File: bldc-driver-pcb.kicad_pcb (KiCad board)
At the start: 4 copper layers, 50 x 50 mm, 75 parts, among them IC1 ATSAMD21G18A-AFT, IC2 AS5047P-ATSM, IC3 L6498D, IC4 L6498D, IC5 L6498D, IC6 AD8030ARZ, IC7 AD8030ARZ, J1 FTSH-105-XX-X-DV, J2 43650-0303, J3 G125-MH11205L1P, J4 USB3135-XX-X_REVB, J5 2159310271, Q1 IPD320N20N3GATMA1, Q2 IPD320N20N3GATMA1, Q3 IPD320N20N3GATMA1, Q4 IPD320N20N3GATMA1, Q5 IPD320N20N3GATMA1, Q6 IPD320N20N3GATMA1

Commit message: More routing
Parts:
- added C16: 0.1u, Capacitor_SMD:C_0402_1005Metric, F.Cu at (143.3, 103.6)
- added D1: ~, Diode_SMD:D_0603_1608Metric, B.Cu at (145.5, 108.9)
- added D2: ~, Diode_SMD:D_0603_1608Metric, B.Cu at (145.4, 113.7)
- added D3: ~, Diode_SMD:D_0603_1608Metric, B.Cu at (141.8, 117.9)
- added D4: ~, Diode_SMD:D_0603_1608Metric, B.Cu at (139.8, 122.4)
- added D5: ~, Diode_SMD:D_0603_1608Metric, B.Cu at (117.6, 91.3)
- added D6: ~, Diode_SMD:D_0603_1608Metric, B.Cu at (131.4, 97.8)
- added R31: 10k, Resistor_SMD:R_0603_1608Metric, B.Cu at (143.0, 106.7)
- added R32: 10k, Resistor_SMD:R_0603_1608Metric, B.Cu at (139.9, 112.0)
- added R33: 10k, Resistor_SMD:R_0603_1608Metric, B.Cu at (137.4, 120.8)
- added R34: 10k, Resistor_SMD:R_0603_1608Metric, B.Cu at (138.0, 123.5)
- added R35: 10k, Resistor_SMD:R_0603_1608Metric, B.Cu at (118.8, 97.0)
- added R36: 10k, Resistor_SMD:R_0603_1608Metric, B.Cu at (126.5, 99.0)
- C1, C15, C2, C3, C4, C5, C6, C7, C8, C9, Cboot1, Cboot2, Cboot3, R1, R10, R11, R12, R13, R14, R15, R16, R17, R18, R19, R2, R20, R21, R22, R23, R24, R25, R26, R27, R29, R3, R30, R4, R5, R6, R7, R8, R9: moved to B.Cu
- C10, C11, C12, C14: footprint Capacitor_SMD:C_0603_1608Metric -> Capacitor_SMD:C_0402_1005Metric
- C13: footprint Capacitor_SMD:C_0603_1608Metric -> Capacitor_SMD:C_0402_1005Metric; moved to B.Cu
- FB1: footprint Inductor_SMD:L_0603_1608Metric -> Inductor_SMD:L_0402_1005Metric
- Rshunt1, Rshunt2, Rshunt3: footprint Resistor_SMD:R_0805_2012Metric -> Resistor_SMD:R_1206_3216Metric; moved to B.Cu
- moved R26 110.8 mm to (95.3, 90.8), turned to 180 degrees
- moved R27 110.8 mm to (95.3, 93.3), turned to 180 degrees
- moved R24 103.7 mm to (99.5, 91.0), turned to 180 degrees
- moved R25 100.8 mm to (103.6, 86.9), turned to 180 degrees
- moved R23 99.3 mm to (103.4, 91.7), turned to 180 degrees
- moved R29 99.0 mm to (108.2, 86.4), turned to 180 degrees
- moved R30 99.0 mm to (108.2, 88.9), turned to 180 degrees
- moved Rshunt2 88.9 mm to (128.9, 123.6), turned to 180 degrees
- moved C9 87.1 mm to (107.9, 92.9), turned to 180 degrees
- moved R14 83.6 mm to (119.2, 93.1), turned to 180 degrees
- moved C8 83.4 mm to (111.4, 91.7), turned to 180 degrees
- moved R12 82.7 mm to (120.7, 91.3), turned to 180 degrees
- moved R21 77.9 mm to (127.0, 119.5), turned to 180 degrees
- moved R22 77.6 mm to (127.0, 121.1)
- moved Rshunt1 75.5 mm to (136.6, 106.0), turned to 90 degrees
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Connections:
- IC3 pad 2: /Microcontroller/TCC0_WO1 -> /Microcontroller/TCC0_WO4
- IC4 pad 1: /Microcontroller/TCC0_WO2 -> /Microcontroller/TCC0_WO1
- IC4 pad 2: /Microcontroller/TCC0_WO4 -> /Microcontroller/TCC0_WO5
- IC5 pad 1: /Microcontroller/TCC0_WO5 -> /Microcontroller/TCC0_WO2
- Q2 pad 3: Net-(Q2-S) -> /Current Sensing/CSA_1_IN+
- Q4 pad 3: Net-(Q4-S) -> /Current Sensing/CSA_2_IN+
- Q6 pad 3: Net-(Q6-S) -> /Current Sensing/CSA_3_IN+
- R18 pad 2: /Current Sensing/CSA_2_IN- -> GND
- R23 pad 1: /Current Sensing/CSA_3_IN- -> GND
- R3 pad 1: /Current Sensing/CSA_1_IN- -> GND
- Rshunt1 pad 1: Net-(Q2-S) -> /Current Sensing/CSA_1_IN+
- Rshunt1 pad 2: /Current Sensing/CSA_1_IN+ -> GND
- Rshunt2 pad 1: Net-(Q4-S) -> /Current Sensing/CSA_2_IN+
- Rshunt2 pad 2: /Current Sensing/CSA_2_IN+ -> GND
- Rshunt3 pad 1: Net-(Q6-S) -> /Current Sensing/CSA_3_IN+
- Rshunt3 pad 2: /Current Sensing/CSA_3_IN+ -> GND
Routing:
- net +3V3: track 62.0 -> 110.4 mm, vias 5 -> 10
- net /Microcontroller/TCC0_WO1: track 0.00 -> 36.8 mm, vias 0 -> 3
- net /Microcontroller/TCC0_WO5: track 0.00 -> 34.9 mm, vias 0 -> 1
- net GND: track 30.1 -> 56.2 mm, vias 15 -> 70
- net /Microcontroller/TCC0_WO6: track 0.00 -> 22.5 mm, vias 0 -> 1
- net /Current Sensing/CSA_2_VOUT: track 0.00 -> 22.4 mm, vias 0 -> 1
- net /Microcontroller/TCC0_WO2: track 0.00 -> 21.4 mm, vias 0 -> 1
- net /Microcontroller/TCC0_WO0: track 0.00 -> 21.2 mm, vias 0 -> 1
- net VBUS: track 61.3 -> 79.2 mm, vias 0 -> 4
- net /Current Sensing/CSA_1_VOUT: track 0.00 -> 16.6 mm, vias 0 -> 1
- net /Three-Phase Inverter/HALF_BRIDGE_1_OUT: track 24.9 -> 41.3 mm, vias 0 -> 1
- net /Microcontroller/TCC0_WO4: track 0.00 -> 15.9 mm, vias 0 -> 1
- net Net-(D2-A): track 0.00 -> 14.1 mm, vias 0 -> 1
- net Net-(IC4-LVG): track 0.00 -> 12.9 mm
- net /Three-Phase Inverter/HALF_BRIDGE_2_OUT: track 27.3 -> 38.7 mm, vias 0 -> 1
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
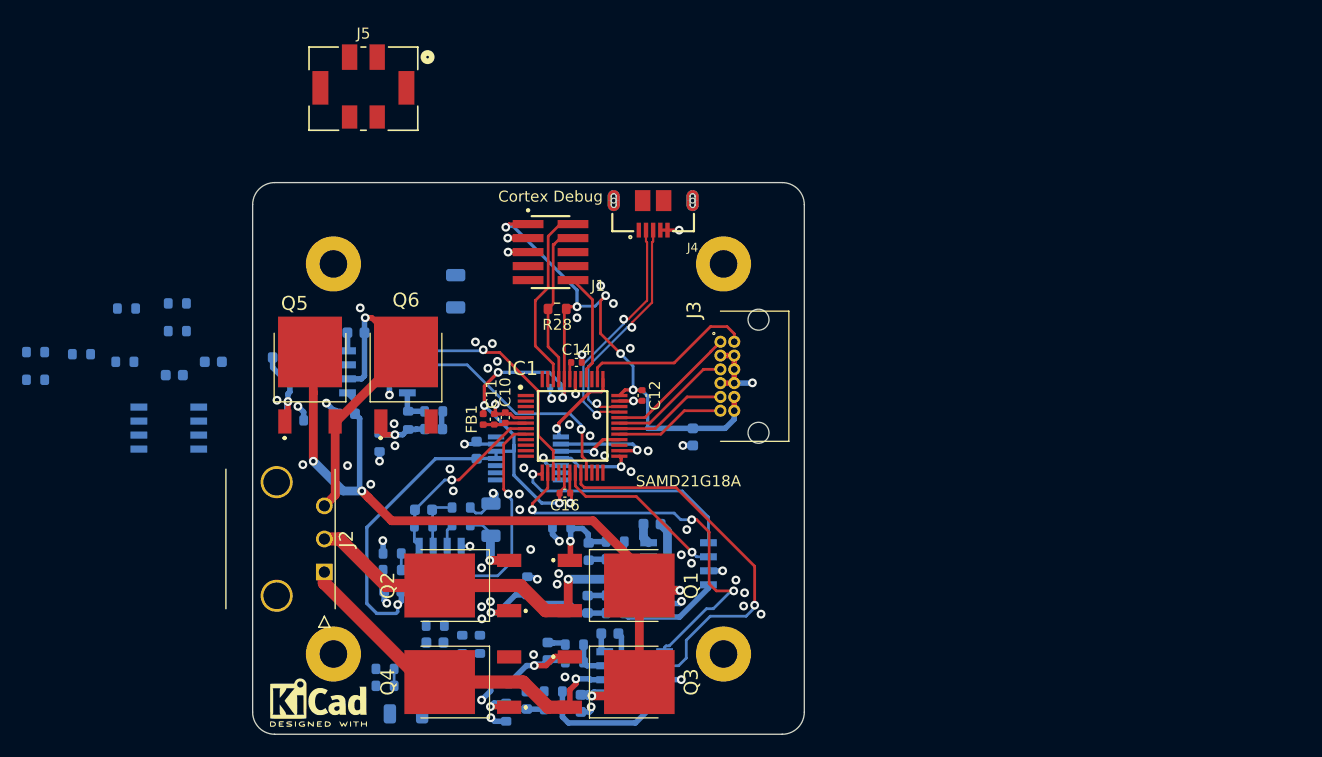
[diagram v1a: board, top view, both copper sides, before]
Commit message: Reroute everything
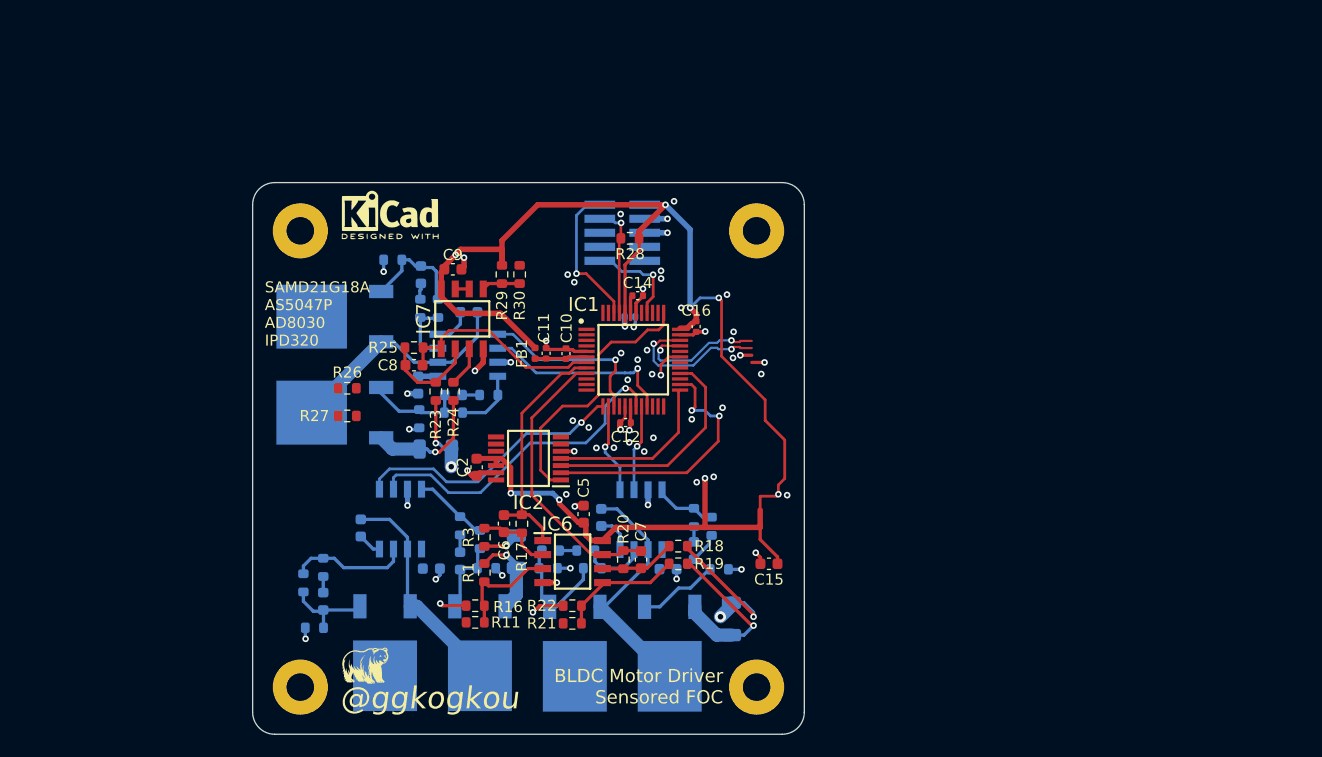
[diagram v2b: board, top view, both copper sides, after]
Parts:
- removed J2: 43650-0303, Sandbox:43650-03YY_03040559
- removed J3: G125-MH11205L1P, Sandbox:G125-MH11205L1P
- removed J4: USB3135-XX-X_REVB, bldc-driver-pcb:GCT_USB3135-XX-X_REVB
- removed J5: 2159310271, Sandbox:CONN_2159310000-SD_02_MOL
- added G***: LOGO, bldc-driver-pcb:Bear, F.Cu at (125.2, 119.2)
- C15, C2, C5, C6, C7, C8, C9, IC2, IC6, IC7, R1, R11, R16, R17, R18, R19, R20, R21, R22, R23, R24, R25, R26, R27, R29, R3, R30: moved to F.Cu
- J1, Q1, Q2, Q3, Q4, Q5, Q6: moved to B.Cu
- moved G*** 44.7 mm to (127.4, 78.4)
- moved R24 33.9 mm to (133.2, 94.4), turned to -90 degrees
- moved R30 31.4 mm to (139.2, 83.8), turned to 90 degrees
- moved Rshunt2 30.7 mm to (158.4, 115.0), turned to 90 degrees
- moved R29 29.5 mm to (137.6, 83.8), turned to -90 degrees
- moved Q1 28.6 mm to (127.0, 123.3), turned to 0 degrees
- moved R2 28.5 mm to (119.6, 111.7), turned to -90 degrees
- moved R26 28.4 mm to (123.6, 94.1), turned to 0 degrees
- moved R27 28.4 mm to (123.6, 96.6), turned to 0 degrees
- moved IC7 28.4 mm to (134.0, 87.8), turned to 90 degrees
- moved R23 28.3 mm to (131.6, 94.4), turned to 90 degrees
- moved C9 27.0 mm to (133.1, 83.3)
- moved R4 26.5 mm to (121.4, 110.3), turned to -90 degrees
- moved Cboot1 26.4 mm to (124.8, 106.8), turned to 90 degrees
- moved R25 26.3 mm to (129.6, 90.4), turned to 0 degrees
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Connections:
- IC1 pad 7: /Current Sensing/CSA_1_VOUT -> /Current Sensing/CSA_3_VOUT
- IC1 pad 8: /Current Sensing/CSA_2_VOUT -> /Current Sensing/CSA_1_VOUT
- IC1 pad 9: /Current Sensing/CSA_3_VOUT -> /Current Sensing/CSA_2_VOUT
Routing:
- net VBUS: track 79.2 -> 1.80 mm, vias 4 -> 0
- net +3V3: track 110.4 -> 150.5 mm
- net /Microcontroller/TCC0_WO1: track 36.8 -> 8.23 mm, vias 3 -> 1
- net /Microcontroller/TCC0_WO5: track 34.9 -> 7.83 mm
- net /Three-Phase Inverter/HALF_BRIDGE_1_OUT: track 41.3 -> 20.5 mm, vias 1 -> 0
- net /Current Sensing/CSA_3_VOUT: track 0.00 -> 19.3 mm
- net /Microcontroller/ENCODER_CSn: track 7.72 -> 24.3 mm, vias 1 -> 0
- net GND: track 56.2 -> 72.5 mm, vias 70 -> 64
- net /Three-Phase Inverter/HALF_BRIDGE_2_OUT: track 38.7 -> 22.4 mm, vias 1 -> 0
- net /Microcontroller/DRV8316_CSn: track 16.0 -> 0.00 mm
- net /Current Sensing/CSA_2_IN+: track 0.00 -> 15.4 mm, vias 0 -> 1
- net /Microcontroller/SERCOM1_PAD1: track 8.86 -> 24.1 mm, vias 1 -> 2
- net /Microcontroller/SERCOM1_PAD3: track 6.02 -> 21.0 mm, vias 1 -> 0
- net /Microcontroller/TCC0_WO4: track 15.9 -> 29.9 mm
- net /Microcontroller/SERCOM3_PAD1: track 12.0 -> 0.00 mm
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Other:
- board text added: "@ggkogkou"
- board text added: "BLDC Motor Driver Sensored FOC"
- board text added: "SAMD21G18A AS5047P AD8030 IPD320"
- board text removed: "Cortex Debug"
- board text removed: "SAMD21G18A"

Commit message: Finalize layout -- VREF pending
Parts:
- added J3: 505567-0671, bldc-driver-pcb:5055670671, B.Cu at (161.8, 100.3)
- added J4: 505567-0671, bldc-driver-pcb:5055670671, B.Cu at (140.0, 79.0)
- added J5: 505567-0471, bldc-driver-pcb:5055670471, B.Cu at (119.1, 106.1)
- added J7: USB3140-30-0170-1-C, bldc-driver-pcb:USB31403001700C, B.Cu at (161.5, 88.4)
- moved C15 4.71 mm to (161.5, 105.3)
- moved R2 3.31 mm to (121.8, 114.2)
- moved J1 2.90 mm to (151.4, 80.0)
- moved R4 2.70 mm to (124.1, 110.4), turned to 180 degrees
- moved D1 1.44 mm to (120.2, 114.2)
- moved R31 0.80 mm to (120.6, 116.6)
- moved Cboot3 0.35 mm to (134.6, 87.5)
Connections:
- net /Microcontroller/RESET renamed /nRST
- net /Microcontroller/SWCLK renamed /SWCLK
- net /Microcontroller/SWDIO renamed /SWDIO
- IC1 pad 24: /Microcontroller/XOUT -> /Microcontroller/ENCODER_CSn
- IC1 pad 30: /Microcontroller/SERCOM5_PAD3 -> /USART5_Tx
- IC1 pad 31: /Microcontroller/SERCOM3_PAD0 -> /USART3_Rx
- IC1 pad 32: /Microcontroller/SERCOM3_PAD1 -> /USART3_Tx
- IC1 pad 37: /Microcontroller/ENCODER_CSn -> unconnected-(IC1-PB22-Pad37)
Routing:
- net VBUS: track 1.80 -> 140.9 mm, vias 0 -> 6
- net /SWDIO: track 13.3 -> 30.0 mm
- net /USART5_Tx: track 0.00 -> 16.0 mm, vias 0 -> 1
- net /USART3_Rx: track 0.00 -> 14.6 mm, vias 0 -> 1
- net /USART3_Tx: track 0.00 -> 13.1 mm, vias 0 -> 1
- net Net-(IC7-+IN_1): track 3.63 -> 16.3 mm
- net /SWCLK: track 10.3 -> 22.9 mm
- net +3V3: track 150.5 -> 138.4 mm, vias 10 -> 7
- net /nRST: track 9.05 -> 17.4 mm
- net GND: track 72.5 -> 79.3 mm, vias 64 -> 101
- net /Microcontroller/ENCODER_CSn: track 24.3 -> 18.4 mm, vias 0 -> 2
- net Net-(D1-K): track 1.46 -> 4.86 mm
- net /Microcontroller/SERCOM3_PAD0: track 2.98 -> 0.00 mm, vias 1 -> 0
- net /Microcontroller/SERCOM1_PAD1: track 24.1 -> 21.7 mm
- net Net-(IC3-HVG): track 10.9 -> 8.65 mm
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- added copper zone on B.Cu, net GND
- added copper zone on B.Cu, net VBUS

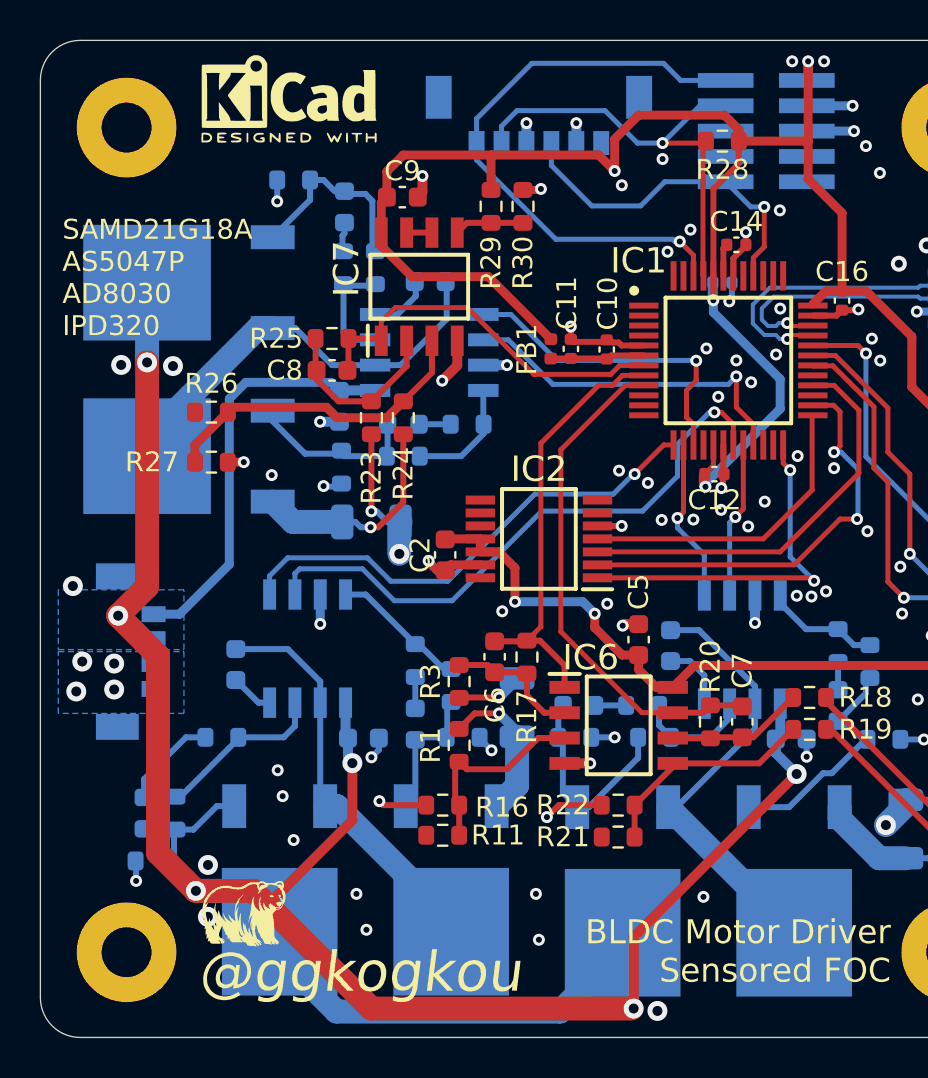
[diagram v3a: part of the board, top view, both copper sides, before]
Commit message: Add connector for motor phases
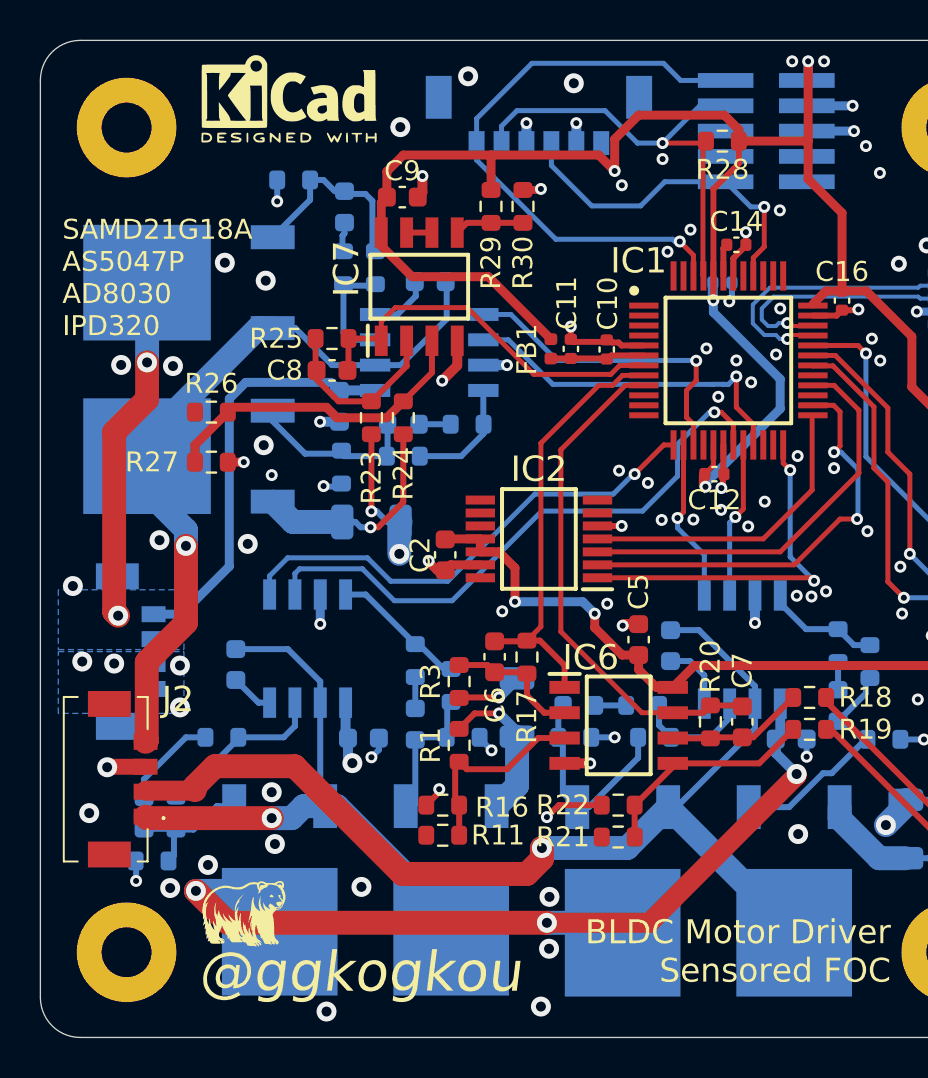
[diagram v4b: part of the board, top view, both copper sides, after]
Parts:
- added J2: 505567-0471, bldc-driver-pcb:5055670471, F.Cu at (118.7, 112.5)
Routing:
- net VBUS: track 140.9 -> 88.7 mm
- net /Three-Phase Inverter/HALF_BRIDGE_2_OUT: track 22.4 -> 53.2 mm, vias 0 -> 1
- net /Three-Phase Inverter/HALF_BRIDGE_3_OUT: track 21.8 -> 37.8 mm, vias 0 -> 1
- net /Three-Phase Inverter/HALF_BRIDGE_1_OUT: track 20.5 -> 29.8 mm, vias 0 -> 1
- net GND: track 79.3 -> 79.9 mm, vias 101 -> 110

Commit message: Fix DRC violations
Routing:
- net VBUS: track 88.7 -> 98.4 mm
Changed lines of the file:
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@@
+	)
+	(segment
+		(start 127.225 105.975)
+		(end 129.035 107.785)
+		(width 0.3)
+		(layer "B.Cu")
+		(net 8)
 	)
 	(segment
@@
 	)
 	(segment
-		(start 127.4105 105.975)
-		(end 129.035 107.5995)
+		(start 124.8 105.975)
+		(end 127.225 105.975)
 		(width 0.3)
 		(layer "B.Cu")
@@
 	)
 	(segment
-		(start 129.035 107.5995)
+		(start 129.035 107.785)
 		(end 129.035 108.662)
 		(width 0.3)
@@
 		(start 129.035 108.662)
 		(end 129.035 113.605)
-		(width 0.3)
-		(layer "B.Cu")
-		(net 8)
-	)
-	(segment
-		(start 124.8 105.975)
-		(end 127.4105 105.975)
 		(width 0.3)
 		(layer "B.Cu")
@@
 	(segment
 		(start 124.474 101.826)
-		(end 122.075 104.225)
+		(end 123.575 102.725)
 		(width 0.45)
 		(layer "B.Cu")
@@
 	)
 	(segment
+		(start 130.305 108.662)
+		(end 130.305 107.755)
+		(width 0.5)
+		(layer "B.Cu")
+		(net 11)
+	)
+	(segment
 		(start 122.8 118.1)
 		(end 124.95 118.1)
@@
 	)
 	(segment
+		(start 130.305 107.755)
+		(end 127.4 104.85)
+		(width 0.5)
+		(layer "B.Cu")
+		(net 11)
+	)
+	(segment
 		(start 130.425 110.438518)
 		(end 130.425 111.474869)
@@
 	)
 	(segment
+		(start 123.575 102.725)
+		(end 122.075 104.225)
+		(width 0.45)
+		(layer "B.Cu")
+		(net 11)
+	)
+	(segment
 		(start 152.105 110.258822)
 		(end 151.876227 110.487595)
@@
 	)
 	(segment
+		(start 125.7 104.85)
+		(end 123.575 102.725)
+		(width 0.5)
+		(layer "B.Cu")
+		(net 11)
+	)
+	(segment
 		(start 129.997487 93.025)
 		(end 129.572487 92.6)
@@
 		(layer "B.Cu")
 		(net 11)
+	)
+	(segment
+		(start 127.4 104.85)
+		(end 125.7 104.85)
+		(width 0.5)
+		(layer "B.Cu")
+		(net 11)

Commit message: Add some silkscreen
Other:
- board text added: "Motor Phases"
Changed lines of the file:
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@@
 		)
+	)
+	(gr_line
+		(start 122 110.5)
+		(end 123.5 110.5)
+		(stroke
+			(width 0.1)
+			(type default)
+		)
+		(layer "F.SilkS")
+	)
+	(gr_line
+		(start 123.5 110.5)
+		(end 123.5 113)
+		(stroke
+			(width 0.1)
+			(type default)
+		)
+		(layer "F.SilkS")
+	)
+	(gr_line
+		(start 123.5 113)
+		(end 123.5 114.5)
+		(stroke
+			(width 0.1)
+			(type default)
+		)
+		(layer "F.SilkS")
+	)
+	(gr_line
+		(start 123.5 114.5)
+		(end 122 114.5)
+		(stroke
+			(width 0.1)
+			(type default)
+		)
+		(layer "F.SilkS")
+	)
+	(gr_line
+		(start 123.5 113)
+		(end 122 113)
+		(stroke
+			(width 0.1)
+			(type default)
+		)
+		(layer "F.SilkS")
+	)
+	(gr_line
+		(start 123.5 113)
+		(end 124 113)
+		(stroke
+			(width 0.1)
+			(type default)
+		)
+		(layer "F.SilkS")
 	)
 	(gr_circle
@@
 		(layer "Edge.Cuts")
 	)
+	(gr_text "Motor\nPhases"
+		(at 124.15 114.85 0)
+		(layer "F.SilkS")
+		(effects
+			(font
+				(size 1.5 1.5)
+				(thickness 0.2)
+				(bold yes)
+			)
+			(justify left bottom)
+		)
+	)
 	(gr_text "BLDC Motor Driver\nSensored FOC"
